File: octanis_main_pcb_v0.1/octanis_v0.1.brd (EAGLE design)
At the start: 94.9 x 30 mm, 83 parts, among them IC1 REG1117, IC2 MPU-6050, Q1 32.768kHz, T1 BC547, T2 BC547, U1 BQ24210, U2 BQ27510_DRZ_12, U3 DRV8836DSSR, U4 DRV8836DSSR, U5 DRV8836DSSR, U6 MSP430F5529IPNR, U7 DRV8836DSSR, U9 BMP180

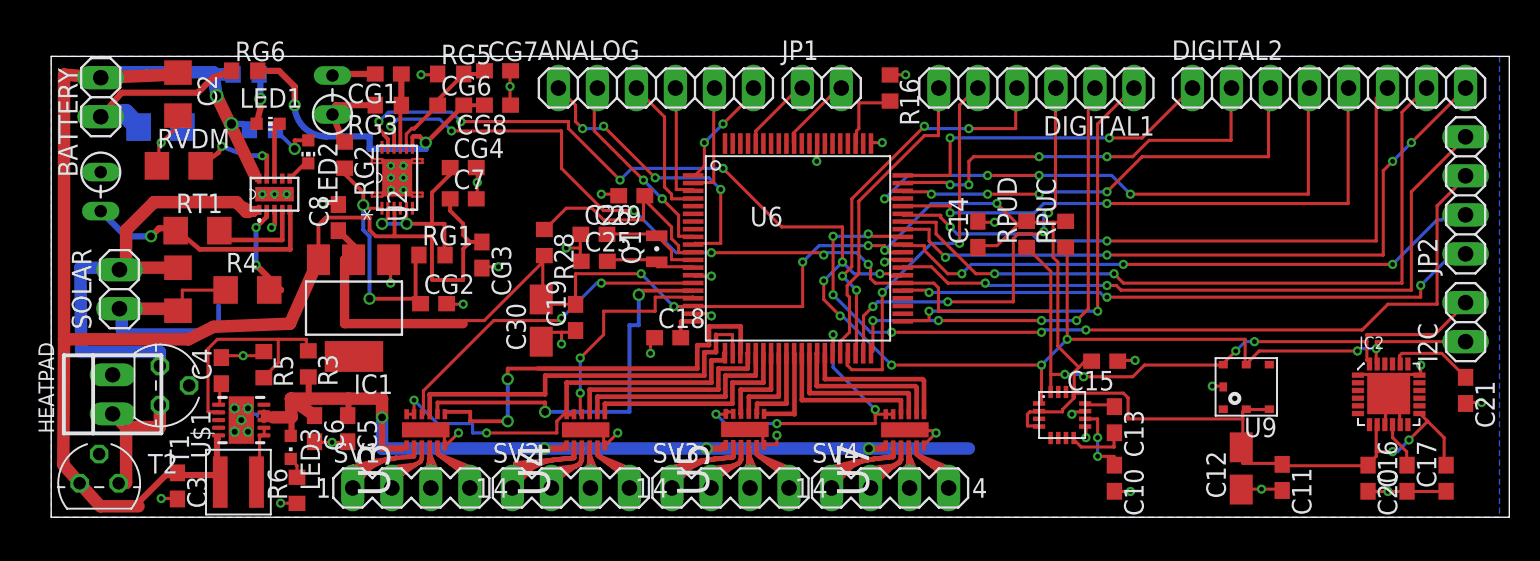
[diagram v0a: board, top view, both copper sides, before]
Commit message: corrected silk layer
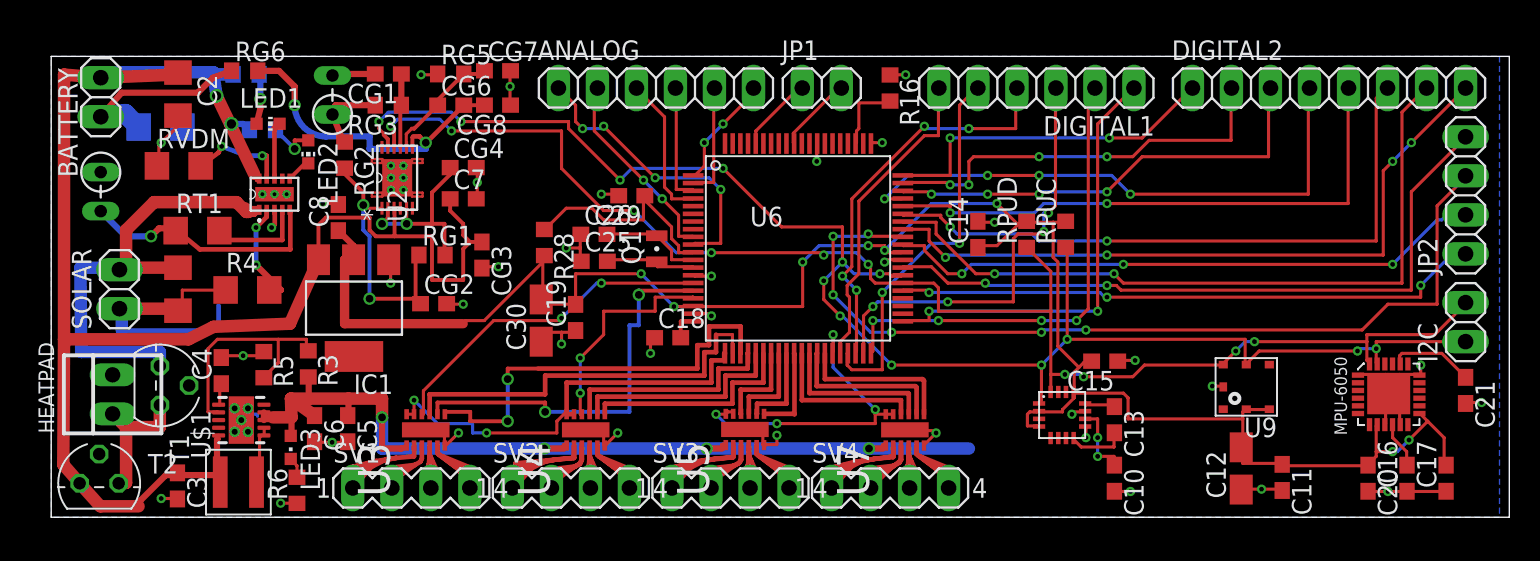
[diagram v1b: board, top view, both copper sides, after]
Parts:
- BATTERY: value BAT -> - BAT +
- C10: value 4.7µ -> 4.7uF
- C13: value 0.22µ -> 0.22uF
- C15: value 0.1µ -> 0.1uF
- COMPASS: value HMC5883L -> HMC5883L
- HEATPAD: value 22-23-2021 -> HEATPAD
- I2C: value I2C -> SCL SDA
- JP1: value SBW -> d SBW clk
- LED3: value (none) -> 5V-ok
- RG1: value (none) -> 1.8M
- RG2: value (none) -> 18.2k
- SOLAR: value SOLAR -> - SOLAR +
- renumbered IC2 to MPU-6050
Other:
- board text added: "HMC5883L"

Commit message: increased space between traces, connected ch_en and 5Ven to uC
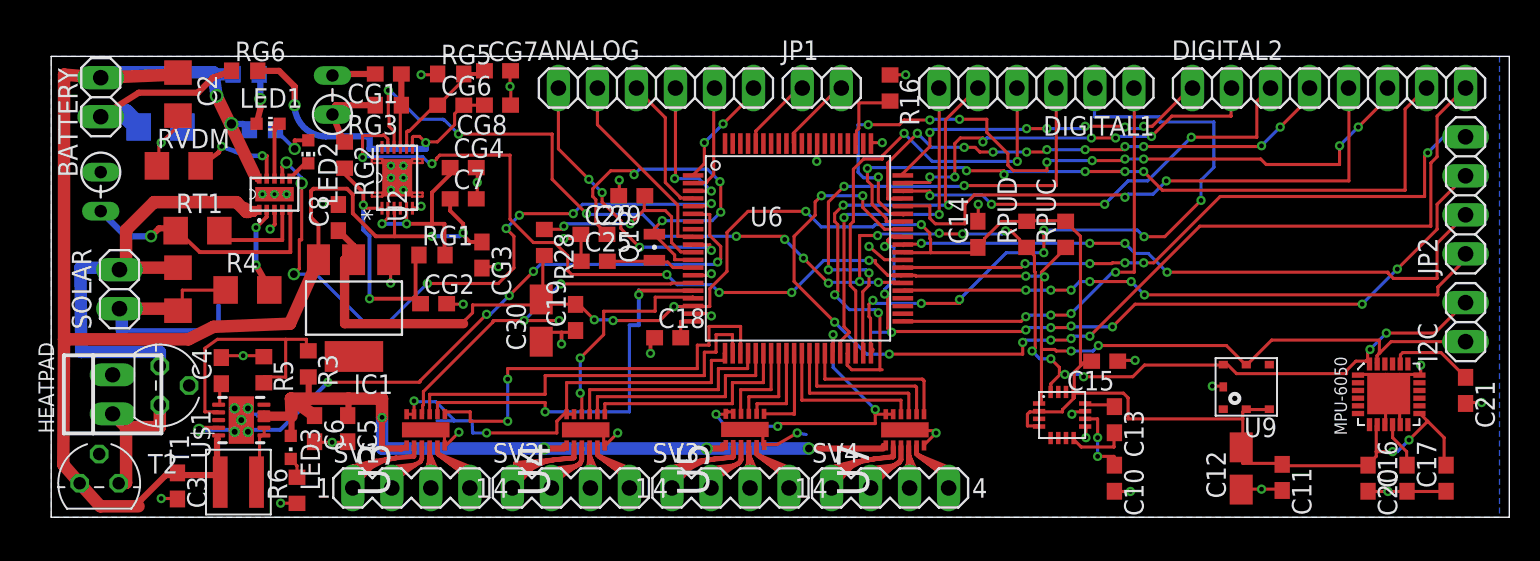
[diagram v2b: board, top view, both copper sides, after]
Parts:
- moved R5 0.33 mm to (13.8, 9.60)
- moved Q1 0.18 mm to (39.3, 17.6)
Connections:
- removed net EN: U1.7
- removed net EN5V: U$1.9
- new net 5VEN: U$1.9, U6.6
- new net CHG_EN: U1.7, U6.5
- net GND: now also U2.V, U2.V_2, U2.V_3, U2.V_4, U2.V_5, U2.V_6
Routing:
- net CHG_EN: track 0.00 -> 44.7 mm, vias 0 -> 8
- net 5VEN: track 0.00 -> 44.2 mm, vias 0 -> 6
- net N$26: track 45.6 -> 70.3 mm, vias 4 -> 8
- net P5.4/XIN: track 6.67 -> 23.4 mm, vias 0 -> 4
- net P3.3: track 31.1 -> 44.9 mm, vias 4 -> 7
- net N$23: track 42.0 -> 49.2 mm, vias 2 -> 10
- net SDA: track 93.8 -> 100.6 mm, vias 10 -> 19
- net P3.0: track 25.2 -> 32.0 mm, vias 2 -> 4
- net GND: track 106.1 -> 112.6 mm, vias 37 -> 38
- net RX: track 58.8 -> 52.4 mm, vias 6 -> 9
- net P3.2: track 28.8 -> 34.4 mm
- net +5V: track 64.6 -> 59.3 mm
- net P3.1: track 26.1 -> 29.7 mm, vias 4 -> 2
- net +3V3: track 128.1 -> 124.6 mm, vias 8 -> 7
- net SPI_SLAVE_EN: track 45.2 -> 41.8 mm, vias 2 -> 5
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
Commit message: most recent version
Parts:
- R3: value 402k -> 270k
- R5: value 100k -> 68k
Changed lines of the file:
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@@
 <attribute name="VALUE" x="10.4394" y="8.4262" size="0.8128" layer="27" rot="R90"/>
 </element>
-<element name="R3" library="rcl" package="R0603" value="402k" x="16.7386" y="9.9822" smashed="yes" rot="R270">
+<element name="R3" library="rcl" package="R0603" value="270k" x="16.7386" y="9.9822" smashed="yes" rot="R270">
 <attribute name="NAME" x="17.3736" y="10.6172" size="1.27" layer="25" rot="R270"/>
 <attribute name="VALUE" x="15.1892" y="11.2268" size="0.8128" layer="27" rot="R270"/>
 </element>
-<element name="R5" library="rcl" package="R0603" value="100k" x="13.843" y="9.6012" smashed="yes" rot="R270">
+<element name="R5" library="rcl" package="R0603" value="68k" x="13.843" y="9.6012" smashed="yes" rot="R270">
 <attribute name="NAME" x="14.478" y="10.2362" size="1.27" layer="25" rot="R270"/>
 <attribute name="VALUE" x="12.2936" y="10.7188" size="0.8128" layer="27" rot="R270"/>
